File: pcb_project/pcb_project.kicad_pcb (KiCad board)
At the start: 6 copper layers, 246 parts, among them IC1 TPS54325PWPR, IC2 TPS54294PWPR, IC3 IS61WV204816BLL-10TLI, IC4 IS61WV204816BLL-10TLI, J10 M20-9990246, J11 M20-9990246, J12 M20-9990246, J13 Conn_01x10_Pin, J2 FTSH-107-01-F-DV-K, J3 Conn_ST_STDC14, J4 DE15_Socket_HighDensity_Mount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, J5 USB_B_Micro, J6 MEM2052-00-195-00-A, J7 USB_A, J8 M20-9990246, J9 M20-9990246, Q1 BC857BS, Q2 BC847BPN, SW2 SW_SPDT, SW3 SW_SPST, SW4 SW_SPST, U1 XC7A100T-FTG256, U10 TPD1E1B04DPYT, U11 TPD1E1B04DPYT, U12 TPD1E1B04DPYT, U13 TPD1E1B04DPYT, U2 STM32U595VJTx, U3 TPS2041B, U4 D3V3XA4B10LP, U5 TPD1E1B04DPYT, U6 TPD1E1B04DPYT, U7 MAX7221xWG, U8 COM-11405, U9 MT25QL128ABA1ESE-0SIT, Y1 48MHz, Y2 XLH736025.175000I

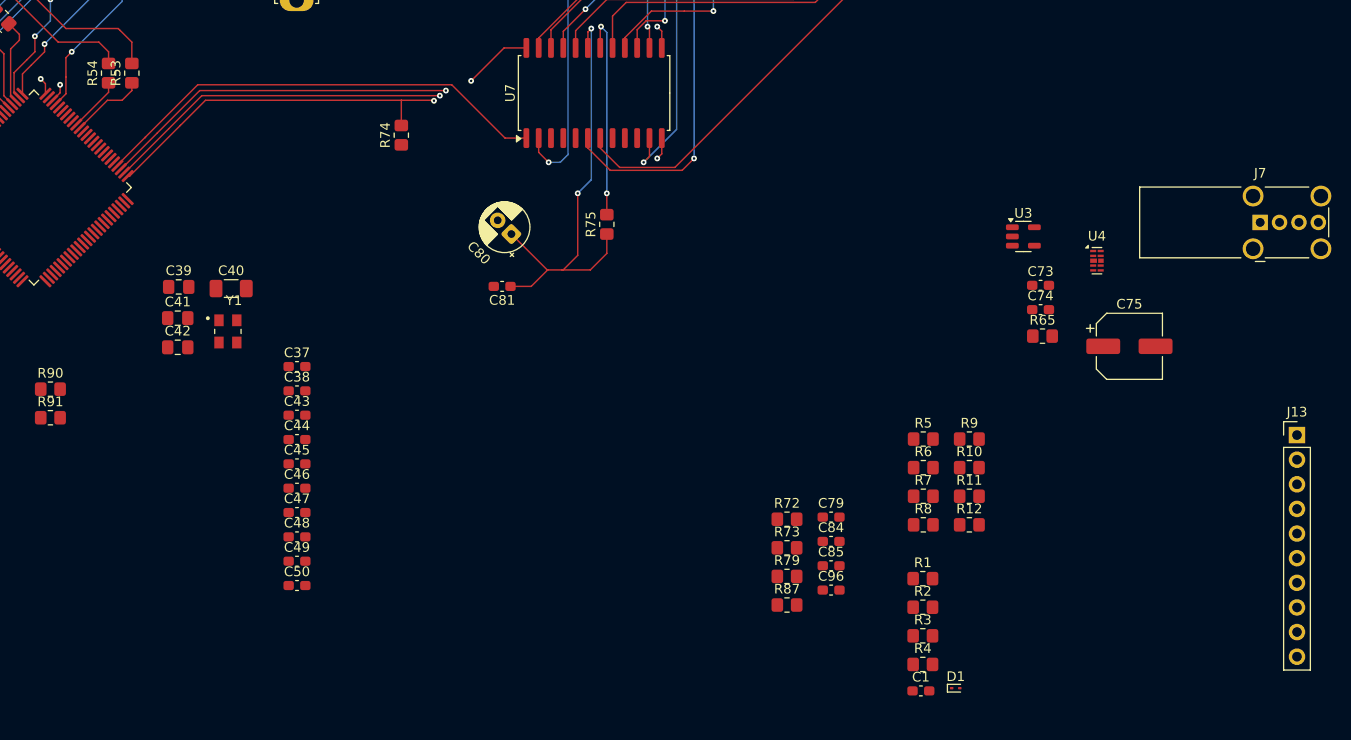
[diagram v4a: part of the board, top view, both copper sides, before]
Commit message: Initial USB Layout, wrong USB footprint
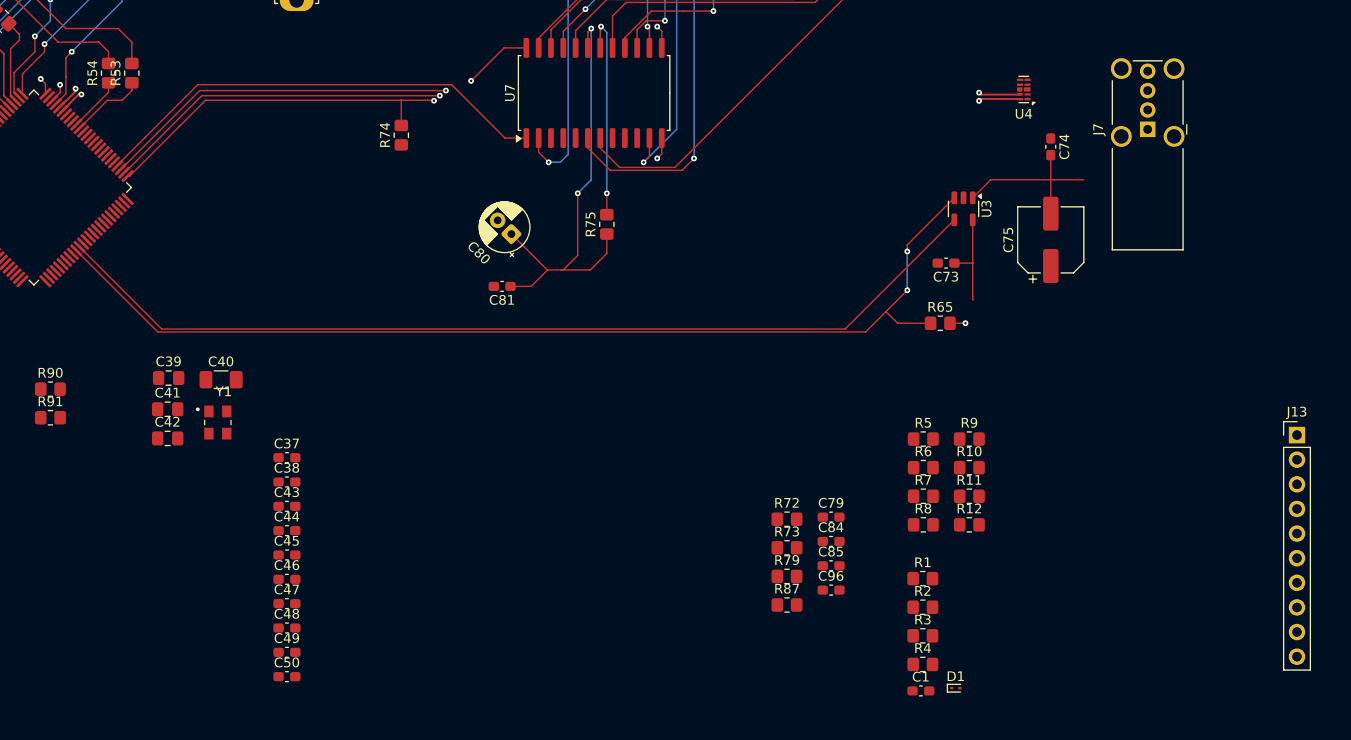
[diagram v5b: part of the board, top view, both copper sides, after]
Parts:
- moved U4 19.2 mm to (244.6, 59.9), turned to 180 degrees
- moved C74 16.8 mm to (247.4, 65.8), turned to -90 degrees
- moved J7 15.1 mm to (257.4, 64.0), turned to 90 degrees
- moved C75 13.7 mm to (247.4, 75.4), turned to 90 degrees
- moved R65 10.6 mm to (236.0, 84.0)
- moved C73 10.0 mm to (236.6, 77.8), turned to 180 degrees
- moved C39 9.46 mm to (156.4, 89.7)
- moved C40 9.46 mm to (161.8, 89.8)
- moved C37 9.46 mm to (168.6, 97.9)
- moved C41 9.46 mm to (156.3, 92.9)
- moved C42 9.46 mm to (156.3, 95.9)
- moved C43 9.46 mm to (168.6, 102.9)
- moved C44 9.46 mm to (168.6, 105.4)
- moved C46 9.46 mm to (168.6, 110.4)
- moved C47 9.46 mm to (168.6, 112.9)
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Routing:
- net /MCU/OTG_HS_D+: track 0.00 -> 117.9 mm, vias 0 -> 2
- net /MCU/OTG_HS_D-: track 0.00 -> 117.4 mm, vias 0 -> 2
- net /MCU/PB0_LPGPIO1_P9: track 0.00 -> 107.6 mm, vias 0 -> 2
- net /MCU/PB1_LPGPIO1_P3: track 0.00 -> 98.4 mm
- net /MCU/PA9_OTG_HS_VBUS: track 0.00 -> 18.3 mm
- net +5V: track 47.0 -> 57.1 mm
- net +3V3: track 44.0 -> 45.6 mm, vias 15 -> 16

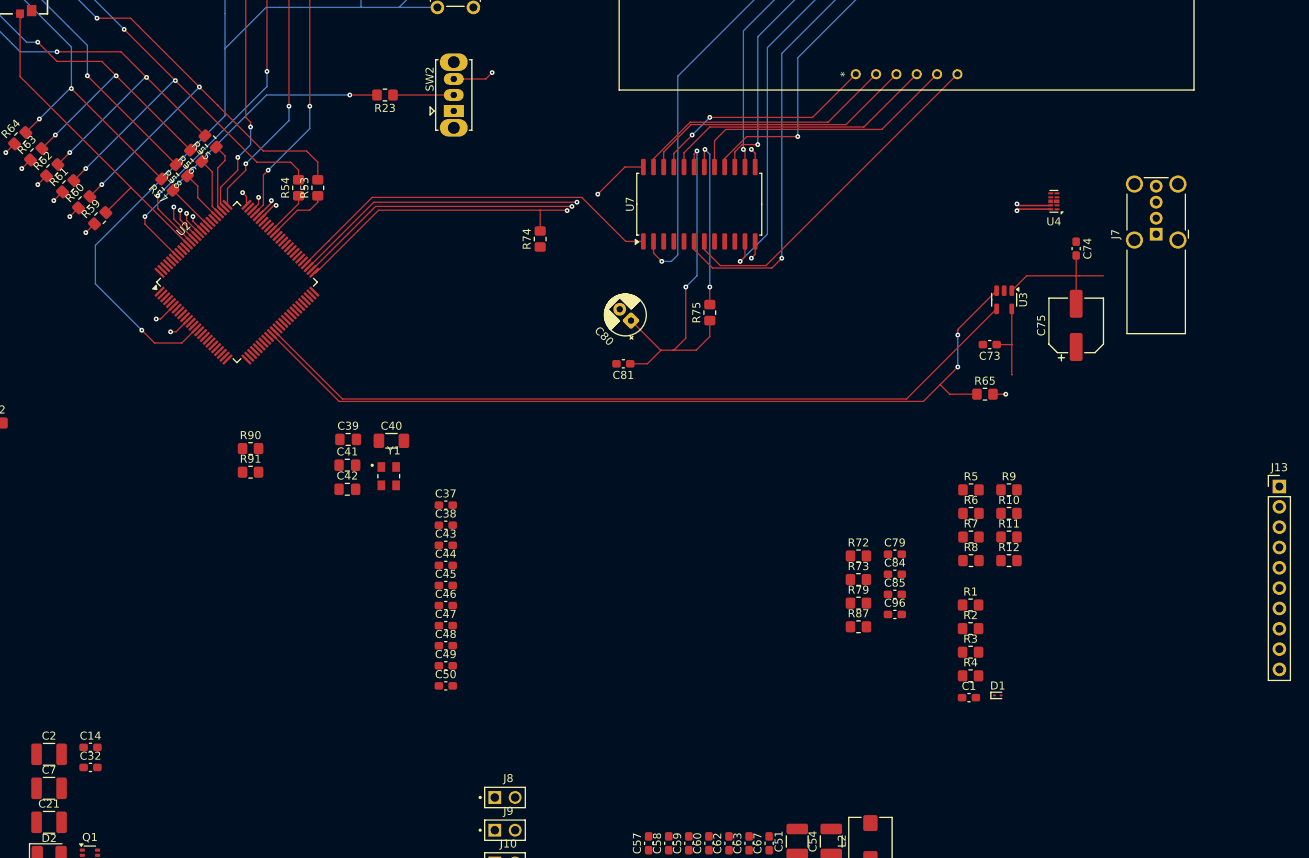
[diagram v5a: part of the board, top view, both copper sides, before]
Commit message: Custom controller layout and some pin changes
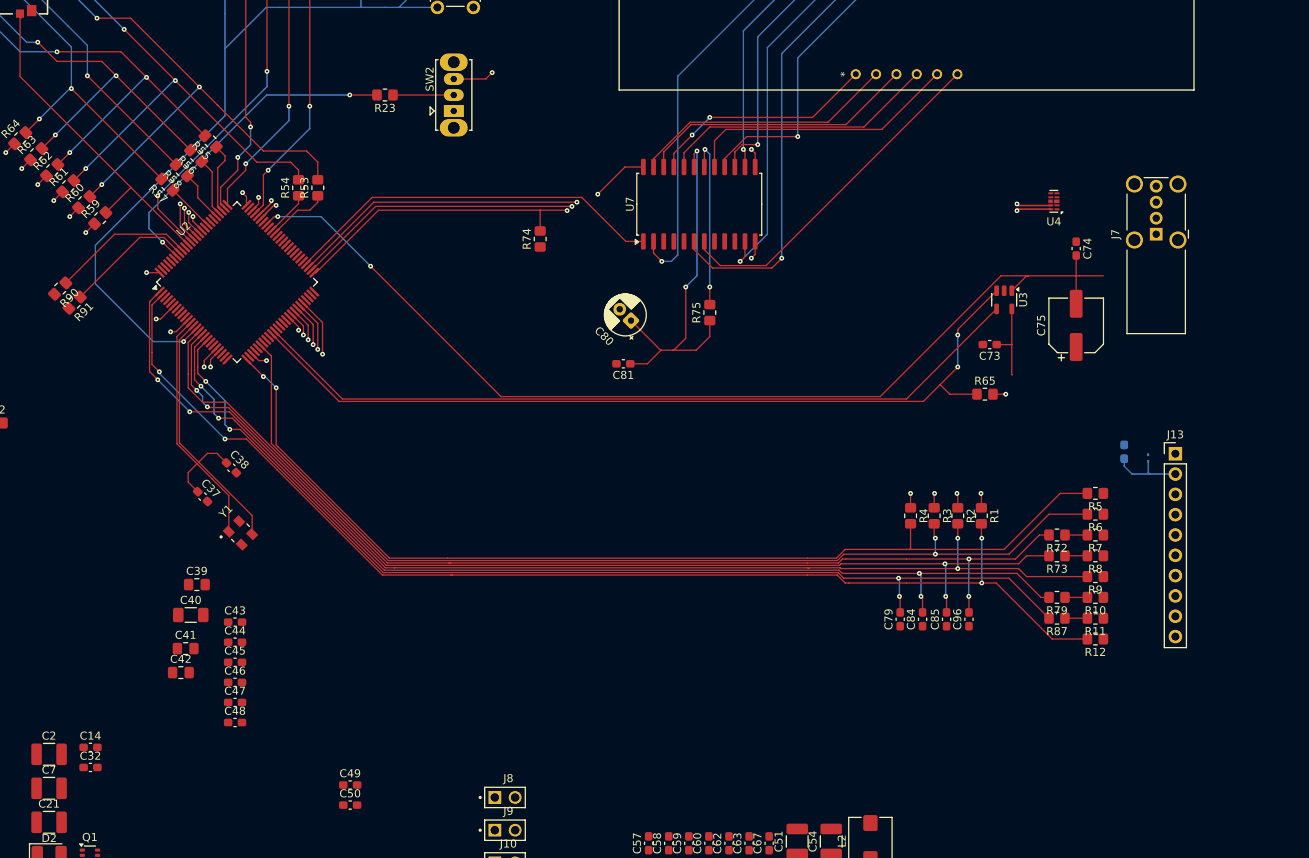
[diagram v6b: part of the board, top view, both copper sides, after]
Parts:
- C1, D1: moved to B.Cu
- moved C1 36.3 mm to (253.4, 91.2), turned to 90 degrees
- moved D1 35.1 mm to (256.4, 92.0), turned to 90 degrees
- moved C40 33.2 mm to (136.7, 111.6)
- moved R90 31.1 mm to (120.4, 70.8), turned to -135 degrees
- moved C42 31.0 mm to (135.5, 118.8)
- moved C41 30.6 mm to (136.1, 115.8)
- moved R91 30.6 mm to (122.2, 72.5), turned to -135 degrees
- moved C37 30.4 mm to (138.2, 96.8), turned to -45 degrees
- moved C45 28.0 mm to (142.3, 117.5)
- moved C48 28.0 mm to (142.3, 125.0)
- moved C43 28.0 mm to (142.3, 112.5)
- moved C44 28.0 mm to (142.3, 115.0)
- moved C46 28.0 mm to (142.3, 120.0)
- moved C47 28.0 mm to (142.3, 122.5)
- moved C38 27.7 mm to (141.8, 93.2), turned to -45 degrees
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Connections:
- R3 pad 2: /MCU/PE0_LPGPIO1_P13 -> /MCU/PA6_LPGPIO1_P2
- R4 pad 2: /MCU/PD13_LPGPIO1_P6 -> /MCU/PA3_LPGPIO1_P1
- R5 pad 2: /MCU/PD13_LPGPIO1_P6 -> /MCU/PA3_LPGPIO1_P1
- R6 pad 2: /MCU/PE0_LPGPIO1_P13 -> /MCU/PA6_LPGPIO1_P2
- U2 pad 26: unconnected-(U2-PA3-Pad26) -> /MCU/PA3_LPGPIO1_P1
- U2 pad 31: unconnected-(U2-PA6-Pad31) -> /MCU/PA6_LPGPIO1_P2
- U2 pad 60: /MCU/PD13_LPGPIO1_P6 -> unconnected-(U2-PD13-Pad60)
- U2 pad 97: /MCU/PE0_LPGPIO1_P13 -> unconnected-(U2-PE0-Pad97)
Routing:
- net /MCU/PE3_LPGPIO1_P15: track 0.00 -> 148.2 mm, vias 0 -> 4
- net /MCU/PE2_LPGPIO1_P14: track 0.00 -> 144.2 mm, vias 0 -> 4
- net /MCU/PC0_ADC1_IN1: track 0.00 -> 132.7 mm, vias 0 -> 2
- net /MCU/PC1_ADC1_IN2: track 0.00 -> 130.5 mm, vias 0 -> 4
- net /MCU/PC2_ADC1_IN3: track 0.00 -> 130.0 mm, vias 0 -> 4
- net /MCU/PC3_ADC1_IN4: track 0.00 -> 129.9 mm, vias 0 -> 4
- net /MCU/PA6_LPGPIO1_P2: track 0.00 -> 127.2 mm, vias 0 -> 2
- net /MCU/PA3_LPGPIO1_P1: track 0.00 -> 126.4 mm, vias 0 -> 2
- net /MCU/PA9_OTG_HS_VBUS: track 18.3 -> 129.5 mm, vias 0 -> 2
- net Net-(U2-PH1): track 0.00 -> 35.0 mm
- net Net-(U2-PH0): track 0.00 -> 33.9 mm
- net +3V3: track 45.6 -> 71.5 mm, vias 16 -> 24
- net Net-(U2-PB6): track 0.00 -> 17.9 mm
- net Net-(U2-PB7): track 0.00 -> 16.3 mm
- net /FPGA/OSPI 3: track 3.00 -> 10.4 mm, vias 0 -> 1
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
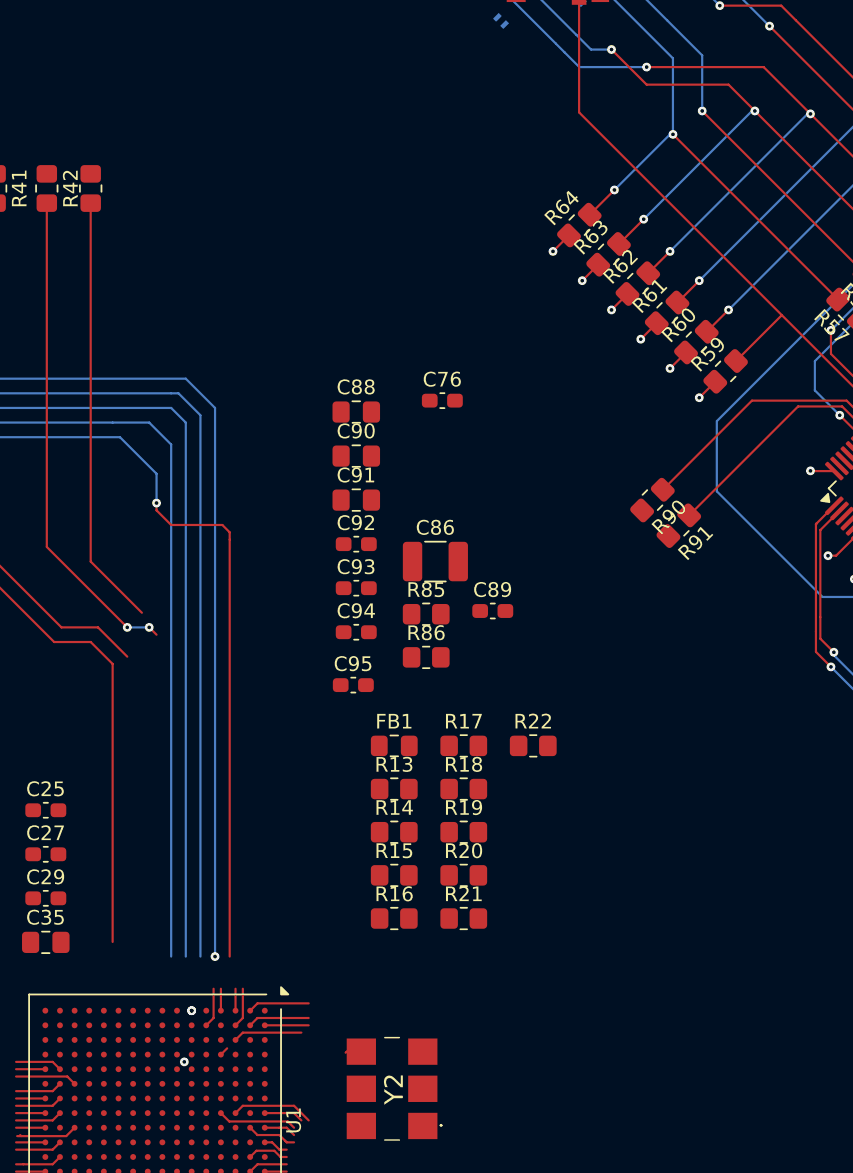
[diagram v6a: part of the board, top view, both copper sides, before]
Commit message: Routed out SPI from FPGA
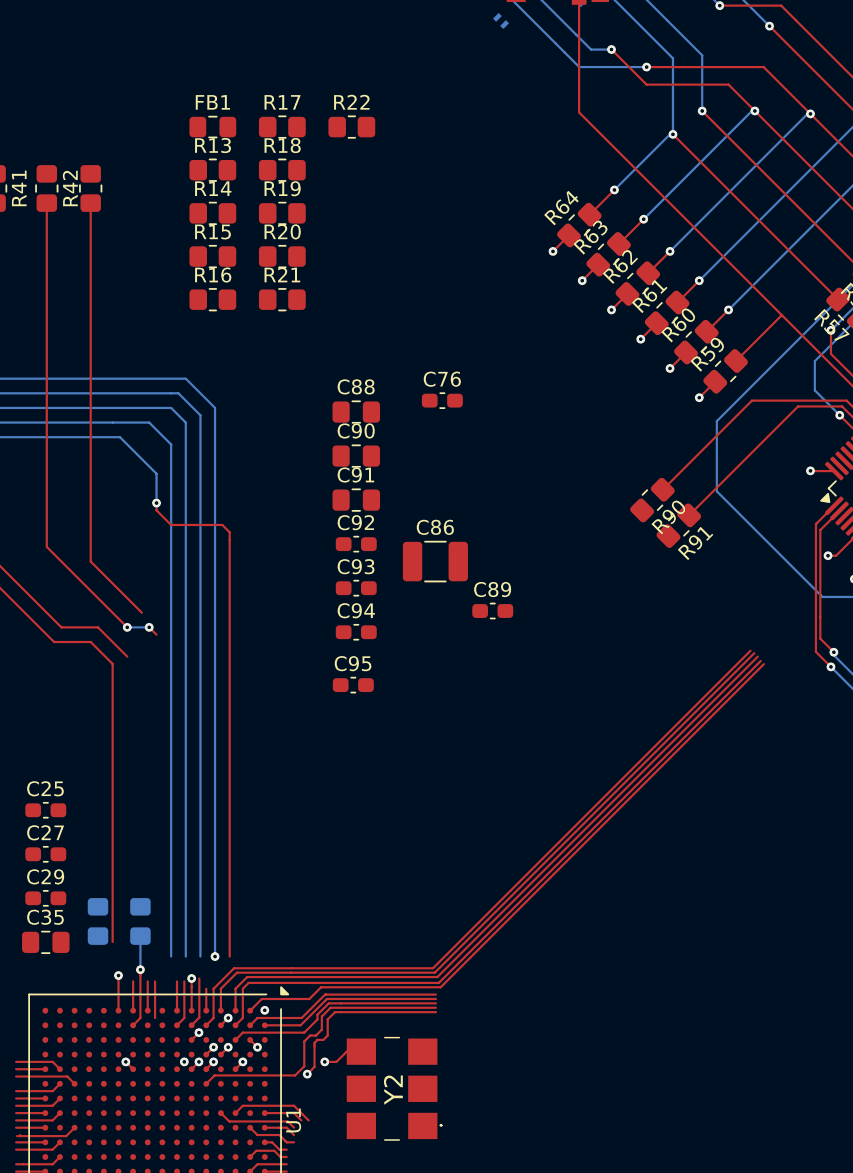
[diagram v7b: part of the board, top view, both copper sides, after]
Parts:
- R85, R86: moved to B.Cu
- moved R15 44.1 mm to (90.3, 54.1)
- moved R16 44.1 mm to (90.3, 57.1)
- moved R20 44.1 mm to (95.1, 54.1)
- moved R21 44.1 mm to (95.1, 57.1)
- moved FB1 44.1 mm to (90.3, 45.3)
- moved R13 44.1 mm to (90.3, 48.2)
- moved R14 44.1 mm to (90.3, 51.2)
- moved R17 44.1 mm to (95.1, 45.3)
- moved R18 44.1 mm to (95.1, 48.2)
- moved R19 44.1 mm to (95.1, 51.2)
- moved R22 44.1 mm to (99.8, 45.3)
- moved R86 28.8 mm to (82.5, 99.6), turned to 90 degrees
- moved R85 28.7 mm to (85.4, 99.6), turned to 90 degrees
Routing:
- net /FPGA/OSPI 6: track 6.80 -> 53.1 mm
- net /FPGA/OSPI 2: track 7.86 -> 53.8 mm
- net /FPGA/OSPI 1: track 6.63 -> 51.7 mm
- net /FPGA/OSPI 5: track 5.85 -> 50.5 mm
- net /FPGA/OSPI 0: track 8.45 -> 49.2 mm
- net /FPGA/OSPI CLK: track 2.14 -> 22.8 mm, vias 1 -> 3
- net /FPGA/OSPI CS: track 3.19 -> 22.6 mm
- net /FPGA/OSPI 7: track 9.76 -> 20.0 mm
- net /FPGA/OSPI 3: track 10.4 -> 19.9 mm
- net /FPGA/OSPI 4: track 6.39 -> 15.8 mm
- net Net-(U1B-IO_L12P_T1_MRCC_35): track 1.71 -> 10.6 mm, vias 0 -> 2
- net Net-(U1B-IO_L24N_T3_35): track 0.00 -> 6.31 mm, vias 0 -> 1
- net +3V3: track 71.5 -> 77.6 mm, vias 24 -> 25
- net GND: track 0.77 -> 4.61 mm, vias 0 -> 4
- net /VGA/R3: track 96.0 -> 99.4 mm
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
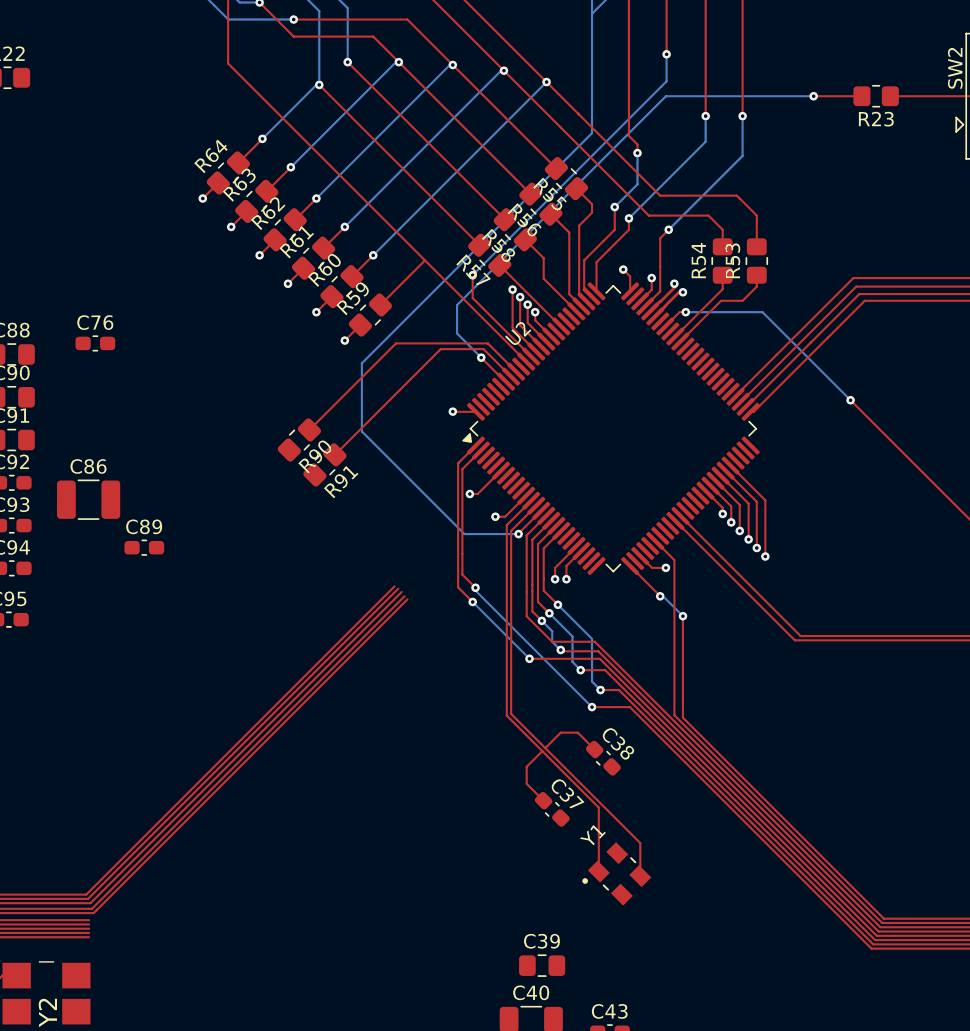
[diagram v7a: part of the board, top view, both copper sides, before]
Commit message: Layout OSPI from MCU
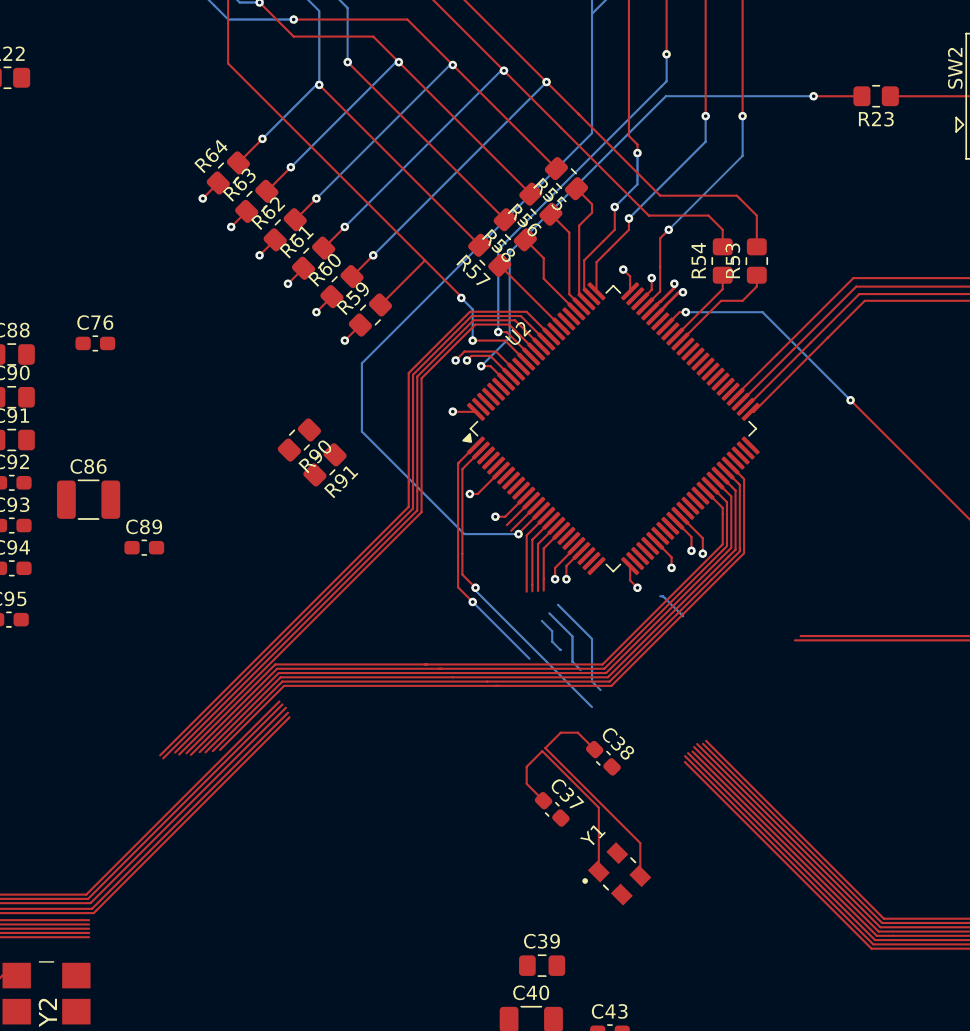
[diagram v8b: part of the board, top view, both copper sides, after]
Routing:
- net /FPGA/OSPI CLK: track 22.8 -> 68.9 mm, vias 3 -> 2
- net /FPGA/OSPI CS: track 22.6 -> 68.1 mm, vias 1 -> 0
- net /FPGA/OSPI 4: track 15.8 -> 60.3 mm, vias 1 -> 0
- net /FPGA/OSPI 3: track 19.9 -> 61.8 mm, vias 1 -> 0
- net /FPGA/OSPI 7: track 20.0 -> 58.9 mm, vias 1 -> 0
- net /FPGA/OSPI 0: track 49.2 -> 81.8 mm, vias 1 -> 0
- net /FPGA/OSPI 1: track 51.7 -> 84.0 mm, vias 1 -> 0
- net /FPGA/OSPI 5: track 50.5 -> 81.9 mm, vias 1 -> 0
- net /FPGA/OSPI 2: track 53.8 -> 85.0 mm, vias 1 -> 0
- net /FPGA/OSPI 6: track 53.1 -> 82.2 mm, vias 1 -> 0
- net /MCU/PC0_ADC1_IN1: track 132.7 -> 115.2 mm
- net Net-(U2-PH0): track 33.9 -> 17.0 mm
- net Net-(U2-PH1): track 35.0 -> 18.7 mm
- net /MCU/PC1_ADC1_IN2: track 130.5 -> 116.0 mm, vias 4 -> 2
- net /MCU/PE2_LPGPIO1_P14: track 144.2 -> 130.0 mm, vias 4 -> 3
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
